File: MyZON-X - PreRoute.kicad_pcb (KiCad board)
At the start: 2 copper layers, 63.5 x 101 mm, 29 parts, among them SW1 SW_DIP_x03, U1 AY-3-8910, U2 74HCT74, U3 74HCT08, U4 74HCT11, U5 74HCT02

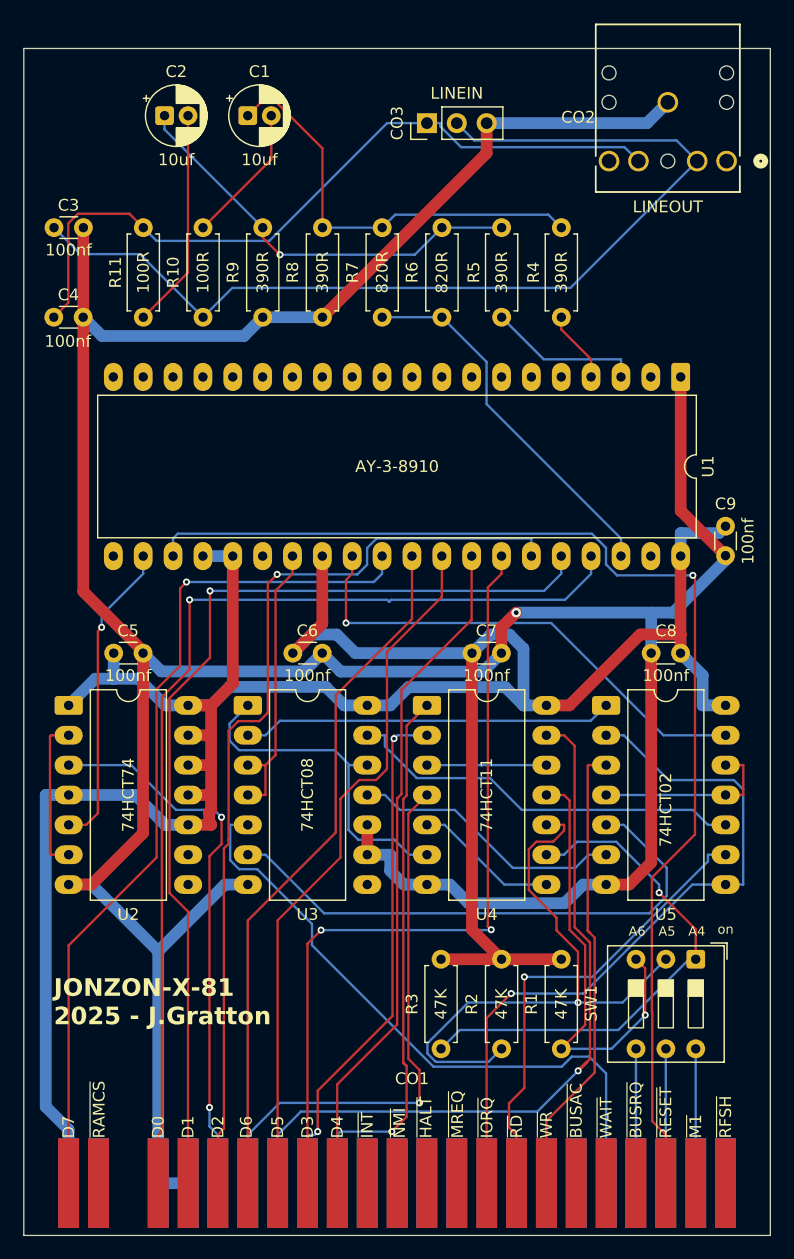
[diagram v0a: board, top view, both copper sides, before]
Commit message: Routed PCB first pass Updated footprint for Audio Line Out Jack Added 3D model for Audio Line Out Jack Updated Schematic PDF Updated 3D Image
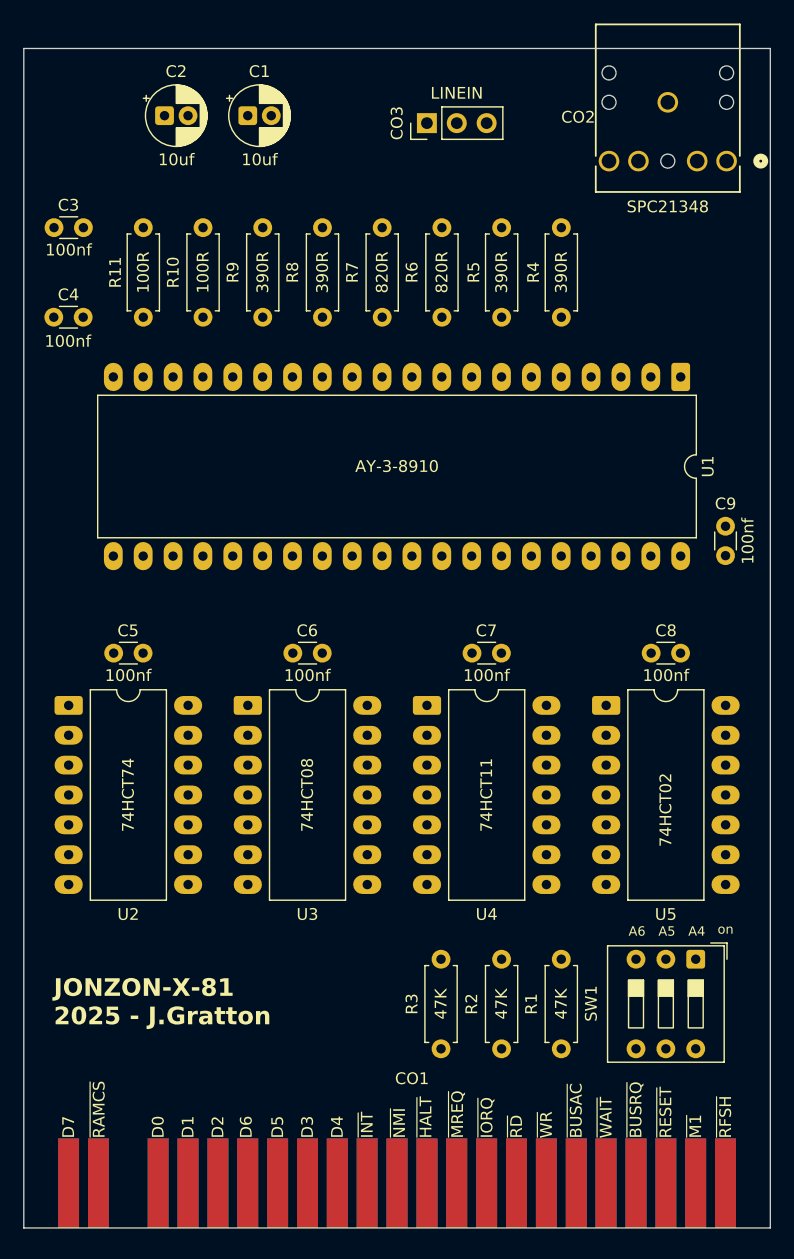
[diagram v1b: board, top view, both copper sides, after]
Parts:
- CO2: value LINEOUT -> SPC21348
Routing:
- net GND: track 289.8 -> 0.00 mm, vias 1 -> 0
- net VCC: track 239.2 -> 0.00 mm
- net /~{RESET}: track 102.0 -> 0.00 mm, vias 1 -> 0
- net /D0: track 87.7 -> 0.00 mm, vias 1 -> 0
- net Net-(CO3-Pin_2): track 85.2 -> 0.00 mm
- net /D1: track 84.4 -> 0.00 mm, vias 1 -> 0
- net /D2: track 80.2 -> 0.00 mm, vias 1 -> 0
- net /D7: track 73.7 -> 0.00 mm, vias 1 -> 0
- net /D3: track 71.4 -> 0.00 mm, vias 2 -> 0
- net /A1: track 67.8 -> 0.00 mm, vias 1 -> 0
- net Net-(CO3-Pin_1): track 63.9 -> 0.00 mm
- net /~{IOREQ}: track 62.2 -> 0.00 mm, vias 1 -> 0
- net /D5: track 60.0 -> 0.00 mm
- net /D6: track 59.1 -> 0.00 mm
- net /D4: track 58.1 -> 0.00 mm
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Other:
- board size 63.5 x 101 mm -> 63.5 x 100.3 mm
